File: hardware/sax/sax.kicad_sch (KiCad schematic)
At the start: 36 parts, among them J101 Cortex, J102 DX07S016JA3, SW101 SKSG, SW102 SKSG, U101 TPS78433QWDRBRQ1, U102 ATSAMD51J, Y101 32k768

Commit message: Refresh
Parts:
- C107, C110: Manufacturer YAGEO -> TDK; Mouser 603-CC603JRNPO9BN180 -> 810-CGA3E2C0G1H180J; Product CC0603JRNPO9BN180 -> CGA3E2C0G1H180J080AA
- INFO101: value (none) -> ~
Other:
- moved on the sheet: FID101, FID102, FID103, H101, ICON101, INFO101, INFO102
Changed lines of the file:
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@@
 	(title_block
 		(title "V2 sax")
-		(date "2026-02-25")
+		(date "2026-03-02")
 		(rev "2026-02-10")
 		(company "Versio Duo")
@@
 	(symbol
 		(lib_id "V2_Production:Layer_Numbers")
-		(at 241.3 168.91 0)
+		(at 213.36 166.37 0)
 		(unit 1)
 		(exclude_from_sim no)
@@
 		(dnp no)
 		(property "Reference" "INFO102"
-			(at 236.22 164.846 0)
+			(at 220.218 166.37 0)
 			(effects
 				(font
@@
 		)
 		(property "Value" "Layer_Numbers"
-			(at 236.22 165.0999 0)
+			(at 208.28 162.5599 0)
 			(effects
 				(font
@@
 		)
 		(property "Footprint" "V2_Production:Layer_Numbers"
-			(at 241.3 175.26 0)
+			(at 213.36 172.72 0)
 			(effects
 				(font
@@
 		)
 		(property "Datasheet" ""
-			(at 241.3 171.45 0)
+			(at 213.36 168.91 0)
 			(effects
 				(font
@@
 		)
 		(property "Description" ""
-			(at 241.3 168.91 0)
+			(at 213.36 166.37 0)
 			(effects
 				(font
@@
 	(symbol
 		(lib_id "V2_Mechanical:MountingHole_2mm")
-		(at 233.68 152.4 0)
+		(at 266.7 173.99 0)
 		(unit 1)
 		(exclude_from_sim no)
@@
 		(fields_autoplaced yes)
 		(property "Reference" "H101"
-			(at 236.22 151.1299 0)
+			(at 269.24 172.7199 0)
 			(effects
 				(font
@@
 		)
 		(property "Value" "2mm"
-			(at 236.22 153.6699 0)
+			(at 269.24 175.2599 0)
 			(effects
 				(font
@@
 		)
 		(property "Footprint" "V2_Mechanical:MountingHole_2mm"
-			(at 233.68 157.48 0)
+			(at 266.7 179.07 0)
 			(effects
 				(font
@@
 		)
 		(property "Datasheet" ""
-			(at 233.68 152.4 0)
+			(at 266.7 173.99 0)
 			(effects
 				(font
@@
 		)
 		(property "Description" "Mounting Hole without connection"
-			(at 233.68 152.4 0)
+			(at 266.7 173.99 0)
 			(effects
 				(font
@@
 			)
 		)
-		(property "Mouser" "603-CC603JRNPO9BN180"
+		(property "Mouser" "810-CGA3E2C0G1H180J"
 			(at 0.762 43.18 0)
 			(show_name yes)
@@
 			)
 		)
-		(property "Product" "CC0603JRNPO9BN180"
+		(property "Product" "CGA3E2C0G1H180J080AA"
 			(at 3.556 43.18 0)
 			(show_name yes)
@@
 			)
 		)
-		(property "Manufacturer" "YAGEO"
+		(property "Manufacturer" "TDK"
 			(at 6.35 43.18 0)
 			(show_name yes)
@@
 	(symbol
 		(lib_id "V2_Production:Revision")
-		(at 213.36 168.91 0)
+		(at 213.36 160.02 0)
 		(unit 1)
 		(exclude_from_sim no)
@@
 		(dnp no)
 		(property "Reference" "INFO101"
-			(at 213.36 164.846 0)
+			(at 224.028 160.02 0)
 			(effects
 				(font
@@
 			)
 		)
-		(property "Value" ""
-			(at 213.36 171.45 0)
+		(property "Value" "~"
+			(at 213.36 162.56 0)
 			(effects
 				(font
@@
 		)
 		(property "Footprint" "V2_Production:Revision"
-			(at 213.36 173.99 0)
+			(at 213.36 165.1 0)
 			(effects
 				(font
@@
 		)
 		(property "Datasheet" ""
-			(at 213.36 168.91 0)
+			(at 213.36 160.02 0)
 			(effects
 				(font
@@
 		)
 		(property "Description" ""
-			(at 213.36 168.91 0)
+			(at 213.36 160.02 0)
 			(effects
 				(font
@@
 	(symbol
 		(lib_id "V2_Mechanical:Fiducial_Paste")
-		(at 269.24 151.13 0)
+		(at 266.7 151.13 0)
 		(unit 1)
 		(exclude_from_sim no)
@@
 		(dnp no)
 		(property "Reference" "FID101"
-			(at 272.034 151.13 0)
+			(at 269.494 151.13 0)
 			(effects
 				(font
@@
 		)
 		(property "Value" "Fiducial_Paste"
-			(at 266.7 147.32 0)
+			(at 264.16 147.32 0)
 			(effects
 				(font
@@
 		)
 		(property "Footprint" "V2_Fiducial:Fiducial_0.5mm_Mask1mm_Paste"
-			(at 269.24 156.21 0)
+			(at 266.7 156.21 0)
 			(effects
 				(font
@@
 		)
 		(property "Datasheet" ""
-			(at 269.24 151.13 0)
+			(at 266.7 151.13 0)
 			(effects
 				(font
@@
 		)
 		(property "Description" "Fiducial Marker"
-			(at 269.24 151.13 0)
+			(at 266.7 151.13 0)
 			(effects
 				(font
@@
 			)
 		)
-		(property "Mouser" "603-CC603JRNPO9BN180"
+		(property "Mouser" "810-CGA3E2C0G1H180J"
 			(at 0.762 38.1 0)
 			(show_name yes)
@@
 			)
 		)
-		(property "Product" "CC0603JRNPO9BN180"
+		(property "Product" "CGA3E2C0G1H180J080AA"
 			(at 3.556 38.1 0)
 			(show_name yes)
@@
 			)
 		)
-		(property "Manufacturer" "YAGEO"
+		(property "Manufacturer" "TDK"
 			(at 6.35 38.1 0)
 			(show_name yes)
@@
 	(symbol
 		(lib_id "V2_Mechanical:Fiducial_Paste")
-		(at 269.24 157.48 0)
+		(at 266.7 157.48 0)
 		(unit 1)
 		(exclude_from_sim no)
@@
 		(dnp no)
 		(property "Reference" "FID102"
-			(at 272.034 157.48 0)
+			(at 269.494 157.48 0)
 			(effects
 				(font
@@
 		)
 		(property "Value" "Fiducial_Paste"
-			(at 270.51 153.67 0)
+			(at 267.97 153.67 0)
 			(effects
 				(font
@@
 		)
 		(property "Footprint" "V2_Fiducial:Fiducial_0.5mm_Mask1mm_Paste"
-			(at 269.24 162.56 0)
+			(at 266.7 162.56 0)
 			(effects
 				(font
@@
 		)
 		(property "Datasheet" ""
-			(at 269.24 157.48 0)
+			(at 266.7 157.48 0)
 			(effects
 				(font
@@
 		)
 		(property "Description" "Fiducial Marker"
-			(at 269.24 157.48 0)
+			(at 266.7 157.48 0)
 			(effects
 				(font
@@
 	(symbol
 		(lib_id "V2_Mechanical:Fiducial_Paste")
-		(at 269.24 163.83 0)
+		(at 266.7 163.83 0)
 		(unit 1)
 		(exclude_from_sim no)
@@
 		(dnp no)
 		(property "Reference" "FID103"
-			(at 272.034 163.83 0)
+			(at 269.494 163.83 0)
 			(effects
 				(font
@@
 		)
 		(property "Value" "Fiducial_Paste"
-			(at 266.7 160.02 0)
+			(at 264.16 160.02 0)
 			(effects
 				(font
@@
 		)
 		(property "Footprint" "V2_Fiducial:Fiducial_0.5mm_Mask1mm_Paste"
-			(at 269.24 168.91 0)
+			(at 266.7 168.91 0)
 			(effects
 				(font
@@
 		)
 		(property "Datasheet" ""
-			(at 269.24 163.83 0)
+			(at 266.7 163.83 0)
 			(effects
 				(font
@@
 		)
 		(property "Description" "Fiducial Marker"
-			(at 269.24 163.83 0)
+			(at 266.7 163.83 0)
 			(effects
 				(font
@@
 	(symbol
 		(lib_id "V2_Artwork:V2-logo")
-		(at 208.28 153.67 0)
+		(at 212.09 151.13 0)
 		(unit 1)
 		(exclude_from_sim no)
@@
 		(dnp no)
 		(property "Reference" "ICON101"
-			(at 204.47 148.082 0)
+			(at 215.9 151.13 0)
 			(effects
 				(font
@@
 		)
 		(property "Value" "V2-logo"
-			(at 204.47 148.59 0)
+			(at 208.28 146.05 0)
 			(effects
 				(font
@@
 		)
 		(property "Footprint" "V2_Artwork:Logo_Small"
-			(at 208.28 161.29 0)
+			(at 212.09 158.75 0)
 			(effects
 				(font
@@
 		)
 		(property "Datasheet" ""
-			(at 208.28 153.67 0)
+			(at 212.09 151.13 0)
 			(effects
 				(font
@@
 		)
 		(property "Description" ""
-			(at 208.28 153.67 0)
+			(at 212.09 151.13 0)
 			(effects
 				(font

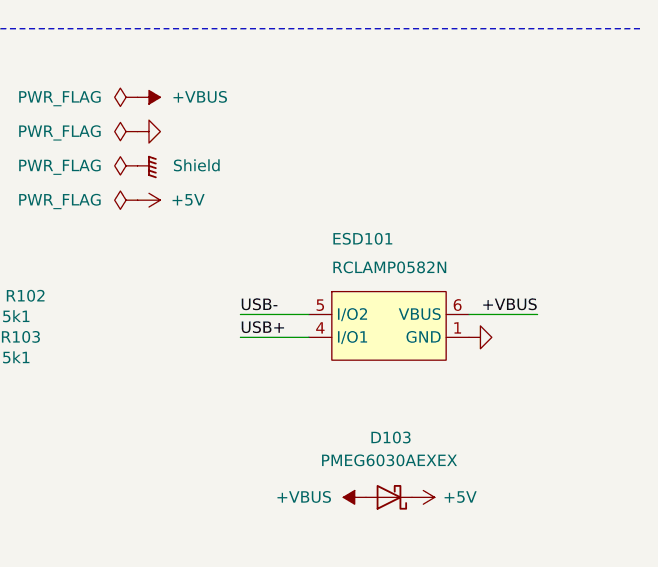
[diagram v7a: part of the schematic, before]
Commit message: Update ESD suppressor
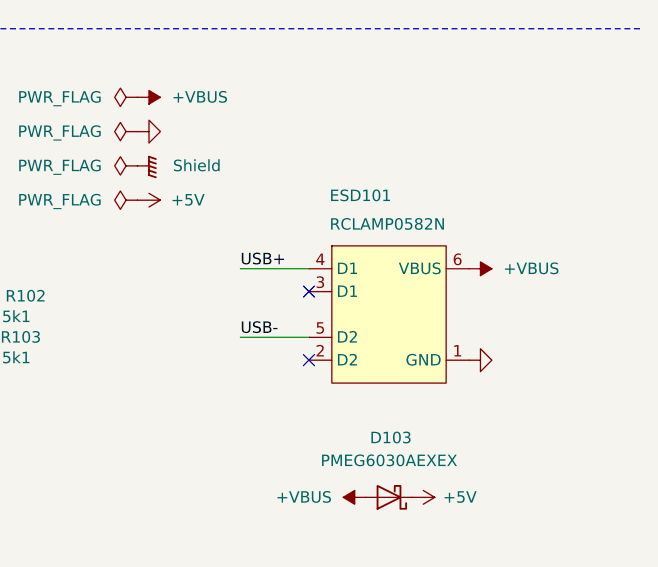
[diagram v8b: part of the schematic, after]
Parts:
- D103, D104, D105: Rating (none) -> 60V
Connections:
- no-connect marks 31 -> 33
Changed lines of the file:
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@@
 	(title_block
 		(title "V2 sax")
-		(date "2026-03-02")
+		(date "2026-03-14")
 		(rev "2026-02-10")
 		(company "Versio Duo")
@@
 	)
 	(no_connect
+		(at 247.65 86.36)
+	)
+	(no_connect
 		(at 53.34 67.31)
 	)
@@
 	)
 	(no_connect
+		(at 247.65 93.98)
+	)
+	(no_connect
 		(at 53.34 44.45)
 	)
@@
 	(wire
 		(pts
-			(xy 240.03 88.9) (xy 247.65 88.9)
+			(xy 240.03 91.44) (xy 247.65 91.44)
 		)
 		(stroke
@@
 	(wire
 		(pts
+			(xy 240.03 83.82) (xy 247.65 83.82)
+		)
+		(stroke
+			(width 0)
+			(type default)
+		)
+	)
+	(wire
+		(pts
 			(xy 53.34 49.53) (xy 31.75 49.53)
 		)
@@
 	(wire
 		(pts
-			(xy 240.03 91.44) (xy 247.65 91.44)
-		)
-		(stroke
-			(width 0)
-			(type default)
-		)
-	)
-	(wire
-		(pts
 			(xy 176.53 162.56) (xy 186.69 162.56)
 		)
@@
 	(wire
 		(pts
-			(xy 265.43 88.9) (xy 273.05 88.9)
-		)
-		(stroke
-			(width 0)
-			(type default)
-		)
-	)
-	(wire
-		(pts
 			(xy 31.75 80.01) (xy 53.34 80.01)
 		)
@@
 		)
 	)
+	(label "USB+"
+		(at 240.03 83.82 0)
+		(effects
+			(font
+				(size 1.27 1.27)
+			)
+			(justify left bottom)
+		)
+	)
 	(label "USB-CC2"
 		(at 203.2 91.44 180)
@@
 		)
 	)
-	(label "+VBUS"
-		(at 273.05 88.9 180)
-		(effects
-			(font
-				(size 1.27 1.27)
-			)
-			(justify right bottom)
-		)
-	)
 	(label "SCL"
 		(at 134.62 152.4 180)
@@
 		)
 	)
-	(label "USB+"
-		(at 240.03 91.44 0)
-		(effects
-			(font
-				(size 1.27 1.27)
-			)
-			(justify left bottom)
-		)
-	)
 	(label "SWDIO"
 		(at 144.78 93.98 180)
@@
 	)
 	(label "USB-"
-		(at 240.03 88.9 0)
+		(at 240.03 91.44 0)
 		(effects
 			(font
@@
 		(dnp no)
 		(property "Reference" "ESD101"
-			(at 250.19 81.28 0)
+			(at 249.936 76.454 0)
 			(effects
 				(font
@@
 		)
 		(property "Value" "RCLAMP0582N"
-			(at 250.19 84.455 0)
+			(at 249.936 79.629 0)
 			(effects
 				(font
@@
 			)
 		)
-		(property "Description" "Unpolarized capacitor, small symbol"
+		(property "Description" ""
 			(at 41.91 172.72 0)
 			(effects
@@
 			)
 		)
-		(property "Description" "Push button switch, generic, two pins"
+		(property "Description" "Push button"
 			(at 247.65 27.94 0)
 			(effects
@@
 			)
 		)
-		(property "Description" "Unpolarized capacitor, small symbol"
+		(property "Description" ""
 			(at 88.9 39.37 0)
 			(effects
@@
 			)
 		)
-		(property "Description" "Two pin crystal, small symbol"
+		(property "Description" ""
 			(at 26.67 40.64 0)
 			(effects
@@
 			)
 		)
-		(property "Description" "Light emitting diode, small symbol"
+		(property "Description" ""
 			(at 132.08 58.42 0)
 			(effects
@@
 			)
 		)
-		(property "Description" "Unpolarized capacitor, small symbol"
+		(property "Description" ""
 			(at 198.12 52.07 0)
 			(effects
@@
 			)
 		)
-		(property "Description" "Unpolarized capacitor, small symbol"
+		(property "Description" ""
 			(at 9.652 43.18 0)
 			(effects
@@
 			)
 		)
-		(property "Description" "Resistor, small symbol"
+		(property "Description" ""
 			(at 219.71 88.9 0)
 			(effects
@@
 			)
 		)
+		(property "Rating" "60V"
+			(at 52.07 138.43 0)
+			(effects
+				(font
+					(size 1.27 1.27)
+				)
+				(hide yes)
+			)
+		)
 		(pin "1"
 		)
@@
 			)
 		)
-		(property "Description" "Unpolarized capacitor, small symbol"
+		(property "Description" ""
 			(at 173.99 52.07 0)
 			(effects
@@
 			)
 		)
-		(property "Description" "Unpolarized capacitor, small symbol"
+		(property "Description" ""
 			(at 119.38 39.37 0)
 			(effects
@@
 			)
 		)
-		(property "Description" "Resistor, small symbol"
+		(property "Description" ""
 			(at 219.71 91.44 0)
 			(effects
@@
 			)
 		)
+		(property "Rating" "60V"
+			(at 256.54 109.22 0)
+			(effects
+				(font
+					(size 1.27 1.27)
+				)
+				(hide yes)
+			)
+		)
 		(pin "1"
 		)
@@
 	)
 	(symbol
+		(lib_id "V2_power:+VBUS")
+		(at 265.43 83.82 270)
+		(unit 1)
+		(exclude_from_sim no)
+		(in_bom yes)
+		(on_board yes)
+		(dnp no)
+		(fields_autoplaced yes)
+		(property "Reference" "#PWR0140"
+			(at 252.73 83.82 0)
+			(effects
+				(font
+					(size 1.27 1.27)
+				)
+				(hide yes)
+			)
+		)
+		(property "Value" "+VBUS"
+			(at 269.24 83.8199 90)
+			(effects
+				(font
+					(size 1.27 1.27)
+					(color 255 92 187 1)
+				)
+				(justify left)
+			)
+		)
+		(property "Footprint" ""
+			(at 265.43 83.82 0)
+			(effects
+				(font
+					(size 1.27 1.27)
+				)
+				(hide yes)
+			)
+		)
+		(property "Datasheet" ""
+			(at 265.43 83.82 0)
+			(effects
+				(font
+					(size 1.27 1.27)
+				)
+				(hide yes)
+			)
+		)
+		(property "Description" "USB Power Delivery"
+			(at 249.936 83.82 0)
+			(effects
+				(font
+					(size 1.27 1.27)
+				)
+				(hide yes)
+			)
+		)
+		(pin "1"
+		)
+		(instances
+			(project "sax"
+				(path "/6c8448b4-b04d-47e1-934e-e40cbe27a7be"
+					(reference "#PWR0140")
+					(unit 1)
+				)
+			)
+		)
+	)
+	(symbol
 		(lib_id "V2_power:Shield")
 		(at 172.72 119.38 0)
@@
 			)
 		)
-		(property "Description" "Resistor, small symbol"
+		(property "Description" ""
 			(at 63.5 120.65 0)
 			(effects
@@
 			)
 		)
-		(property "Description" "Unpolarized capacitor, small symbol"
+		(property "Description" ""
 			(at 9.652 38.1 0)
 			(effects
@@
 			)
 		)
-		(property "Description" "Resistor, small symbol"
+		(property "Description" ""
 			(at 152.4 58.42 0)
 			(effects
@@
 	(symbol
 		(lib_id "V2_power:GND")
-		(at 265.43 91.44 90)
+		(at 265.43 93.98 90)
 		(unit 1)
 		(exclude_from_sim no)
@@
 		(fields_autoplaced yes)
 		(property "Reference" "#PWR125"
-			(at 271.78 91.44 0)
+			(at 271.78 93.98 0)
 			(effects
 				(font
@@
 		)
 		(property "Value" "GND"
-			(at 269.24 91.4399 90)
+			(at 269.24 93.9799 90)
 			(effects
 				(font
@@
 		)
 		(property "Footprint" ""
-			(at 265.43 91.44 0)
+			(at 265.43 93.98 0)
 			(effects
 				(font
@@
 		)
 		(property "Datasheet" ""
-			(at 265.43 91.44 0)
+			(at 265.43 93.98 0)
 			(effects
 				(font
@@
 		)
 		(property "Description" ""
-			(at 265.43 91.44 0)
+			(at 265.43 93.98 0)
 			(effects
 				(font
@@
 			)
 		)
-		(property "Description" "Unpolarized capacitor, small symbol"
+		(property "Description" ""
 			(at 99.06 39.37 0)
 			(effects
@@
 			)
 		)
-		(property "Description" "Unpolarized capacitor, small symbol"
+		(property "Description" ""
 			(at 78.74 39.37 0)
 			(effects
@@
 			)
 		)
-		(property "Description" "Push button switch, generic, two pins"
+		(property "Description" "Push button"
 			(at 133.35 76.2 0)
 			(effects
@@
 			)
 		)
-		(property "Description" "Unpolarized capacitor, small symbol"
+		(property "Description" ""
 			(at 109.22 39.37 0)
 			(effects
@@
 			)
 		)
+		(property "Rating" "60V"
+			(at 256.54 91.44 0)
+			(effects
+				(font
+					(size 1.27 1.27)
+				)
+				(hide yes)
+			)
+		)
 		(pin "1"
 		)
@@
 			)
 		)
-		(property "Description" "Unpolarized capacitor, small symbol"
+		(property "Description" ""
 			(at 57.15 41.91 0)
 			(effects
